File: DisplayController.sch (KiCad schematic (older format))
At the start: 31 parts, among them IC1 LM2937IMP-5.0, IC2 LM2937IMP-3.3, P1 PWR, P2 OUTPUT, P3 Programming Header, Q1 PZT2222A, Q2 PZT2222A, Q3 PZT2222A, Q4 PZT2222A, SW1 RST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

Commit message: WIP: converted ESP footprint to SMD (pads). Now rerouting and changing configuration of signal pins so that signal routing is easier.
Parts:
- U1: value ESP-12E -> ESP-12; footprint ESP8266:ESP-12E -> ESP8266:ESP-12-SMD; symbol ESP-12E -> ESP-12
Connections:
- net GND: now also U1.9 (GND); no longer U1.15 (GND)
- net at U1.10 (GPIO15): now also R13.2
- net at U1.12 (GPIO0): now also R12.2, SW2.2
- net at U1.16 (TXD): now also P3.2 (P2); no longer R13.2
- net at P3.3 (P3): now also U1.15 (RXD); no longer U1.21 (RXD)
- net at U1.4 (GPIO16): now also R4.2; no longer R2.2
- net at U1.5 (GPIO14): now also R2.2; no longer R4.2
- net at U1.6 (GPIO12): now also R8.2; no longer R6.2
- net at U1.7 (GPIO13): now also R6.2; no longer R8.2
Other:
- moved on the sheet: C5, SW1, SW2

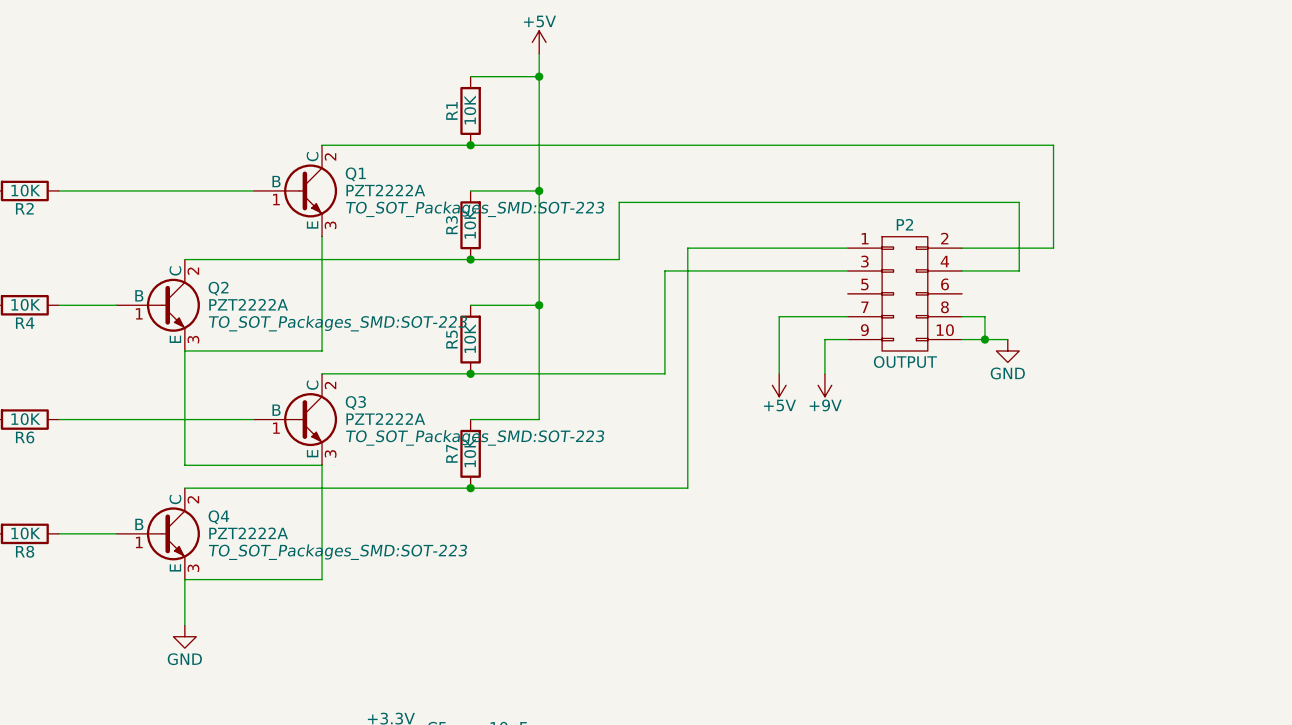
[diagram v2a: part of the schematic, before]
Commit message: Changing SOT-223 footprint to SOT-23-3. Respin and resize of the board.
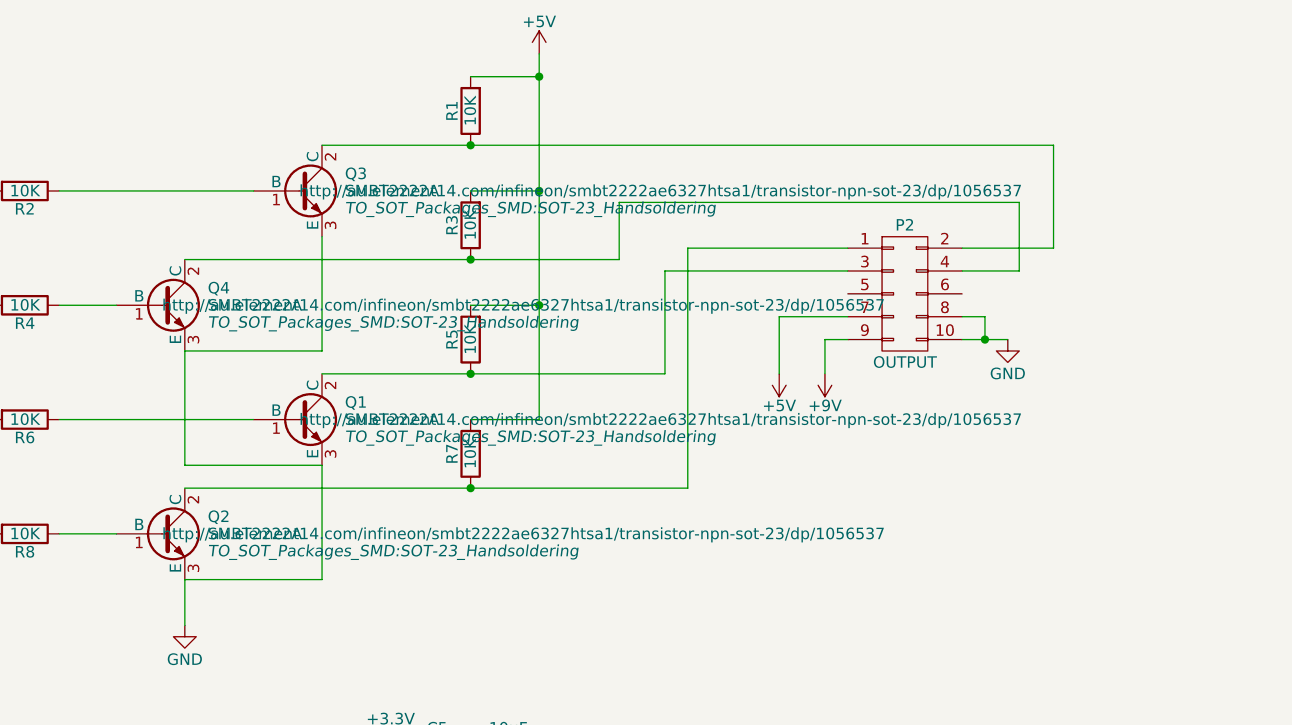
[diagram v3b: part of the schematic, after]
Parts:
- Q1: renamed from Q3; value PZT2222A -> SMBT2222A; footprint TO_SOT_Packages_SMD:SOT-223 -> TO_SOT_Packages_SMD:SOT-23_Handsoldering
- Q2: renamed from Q4; value PZT2222A -> SMBT2222A; footprint TO_SOT_Packages_SMD:SOT-223 -> TO_SOT_Packages_SMD:SOT-23_Handsoldering
- Q3: renamed from Q1; value PZT2222A -> SMBT2222A; footprint TO_SOT_Packages_SMD:SOT-223 -> TO_SOT_Packages_SMD:SOT-23_Handsoldering
- Q4: renamed from Q2; value PZT2222A -> SMBT2222A; footprint TO_SOT_Packages_SMD:SOT-223 -> TO_SOT_Packages_SMD:SOT-23_Handsoldering
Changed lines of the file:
@@
 $EndComp
 $Comp
-L PZT2222A Q2
+L PZT2222A Q4
 U 1 1 5842D47E
 P 6750 1800
-F 0 "Q2" H 6950 1875 50  0000 L CNN
-F 1 "PZT2222A" H 6950 1800 50  0000 L CNN
-F 2 "TO_SOT_Packages_SMD:SOT-223" H 6950 1725 50  0000 L CIN
-F 3 "" H 6750 1800 50  0000 L CNN
+F 0 "Q4" H 6950 1875 50  0000 L CNN
+F 1 "SMBT2222A" H 6950 1800 50  0000 L CNN
+F 2 "TO_SOT_Packages_SMD:SOT-23_Handsoldering" H 6950 1725 50  0000 L CIN
+F 3 "http://au.element14.com/infineon/smbt2222ae6327htsa1/transistor-npn-sot-23/dp/1056537" H 6750 1800 50  0000 L CNN
 	1    6750 1800
 	1    0    0    -1
 $EndComp
 $Comp
-L PZT2222A Q4
+L PZT2222A Q2
 U 1 1 5842D4D1
 P 6750 2800
-F 0 "Q4" H 6950 2875 50  0000 L CNN
-F 1 "PZT2222A" H 6950 2800 50  0000 L CNN
-F 2 "TO_SOT_Packages_SMD:SOT-223" H 6950 2725 50  0000 L CIN
-F 3 "" H 6750 2800 50  0000 L CNN
+F 0 "Q2" H 6950 2875 50  0000 L CNN
+F 1 "SMBT2222A" H 6950 2800 50  0000 L CNN
+F 2 "TO_SOT_Packages_SMD:SOT-23_Handsoldering" H 6950 2725 50  0000 L CIN
+F 3 "http://au.element14.com/infineon/smbt2222ae6327htsa1/transistor-npn-sot-23/dp/1056537" H 6750 2800 50  0000 L CNN
 	1    6750 2800
 	1    0    0    -1
 $EndComp
 $Comp
-L PZT2222A Q1
+L PZT2222A Q3
 U 1 1 5842D512
 P 7350 1300
-F 0 "Q1" H 7550 1375 50  0000 L CNN
-F 1 "PZT2222A" H 7550 1300 50  0000 L CNN
-F 2 "TO_SOT_Packages_SMD:SOT-223" H 7550 1225 50  0000 L CIN
-F 3 "" H 7350 1300 50  0000 L CNN
+F 0 "Q3" H 7550 1375 50  0000 L CNN
+F 1 "SMBT2222A" H 7550 1300 50  0000 L CNN
+F 2 "TO_SOT_Packages_SMD:SOT-23_Handsoldering" H 7550 1225 50  0000 L CIN
+F 3 "http://au.element14.com/infineon/smbt2222ae6327htsa1/transistor-npn-sot-23/dp/1056537" H 7350 1300 50  0000 L CNN
 	1    7350 1300
 	1    0    0    -1
 $EndComp
 $Comp
-L PZT2222A Q3
+L PZT2222A Q1
 U 1 1 5842D53F
 P 7350 2300
-F 0 "Q3" H 7550 2375 50  0000 L CNN
-F 1 "PZT2222A" H 7550 2300 50  0000 L CNN
-F 2 "TO_SOT_Packages_SMD:SOT-223" H 7550 2225 50  0000 L CIN
-F 3 "" H 7350 2300 50  0000 L CNN
+F 0 "Q1" H 7550 2375 50  0000 L CNN
+F 1 "SMBT2222A" H 7550 2300 50  0000 L CNN
+F 2 "TO_SOT_Packages_SMD:SOT-23_Handsoldering" H 7550 2225 50  0000 L CIN
+F 3 "http://au.element14.com/infineon/smbt2222ae6327htsa1/transistor-npn-sot-23/dp/1056537" H 7350 2300 50  0000 L CNN
 	1    7350 2300
 	1    0    0    -1
